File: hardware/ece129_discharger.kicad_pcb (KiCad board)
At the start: 2 copper layers, 102 parts, among them J1 Conn_01x03, J10 Conn_01x02, J11 Conn_02x05_Top_Bottom, J12 Conn_01x08, J13 Conn_02x05_Top_Bottom, J14 Conn_01x02, J16 Conn_01x08, J17 Conn_01x02, J18 Conn_01x02, J19 Conn_01x04, J2 Conn_01x02, J20 Conn_01x02, J3 Conn_01x02, J4 Conn_01x02, J5 Conn_01x02, J6 Conn_01x02, J7 Conn_01x02, J8 Conn_01x02, J9 Conn_01x02, Q2 AO3400A, U1 NUCLEO-H503RB, U13 INA126U/2K5, U15 MCP6004, U16 LTC6992CS6-2-TRMPBF, U17 6N137, U2 SN74LVC1T45DBV, U3 MCP6004, U4 MCP6004, U5 CD4052B, U6 VX7805-500, U7 ISO1050DUB, U8 MCP6004, U9 CC1R5-1205SR-E

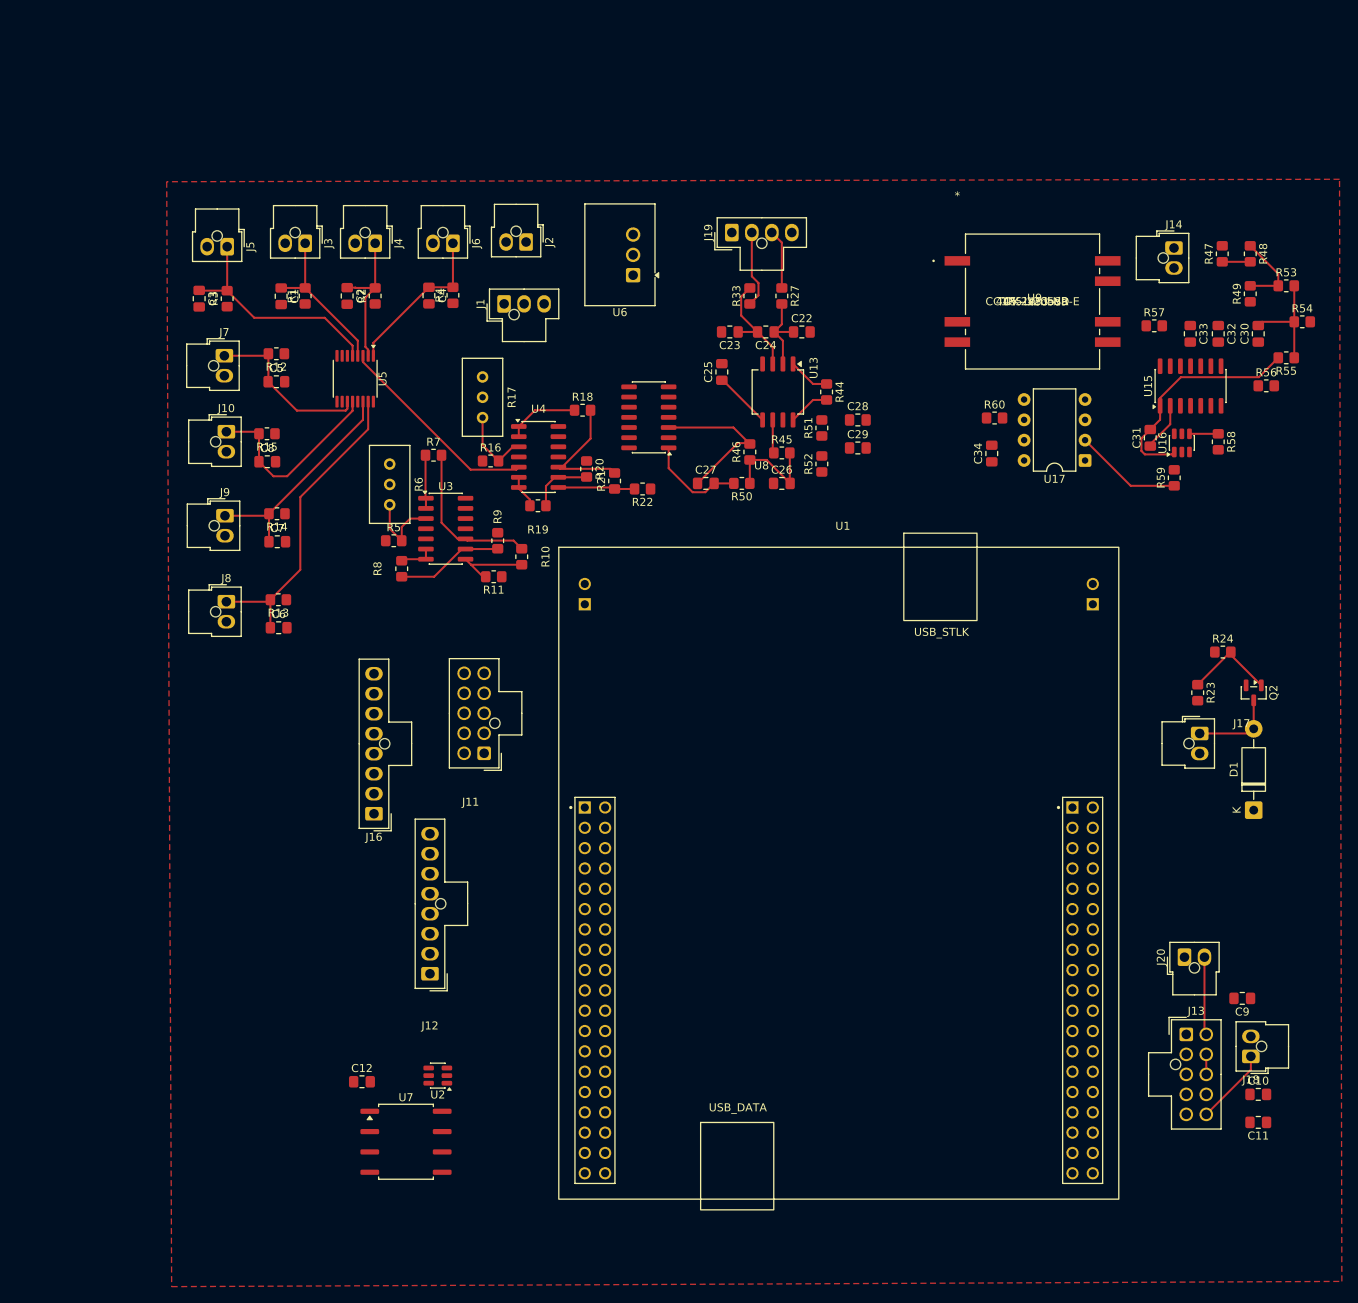
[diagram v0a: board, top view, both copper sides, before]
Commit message: Finished Layout and routing
* Flipped CAN transceiver upside down on schematic
* Moved CAN transceiver nearer to J13 and MCU CAN pins
* Moved 5V DCDC caps nearer to 5V DCDC
* Moved Silkscreen out from under U9
* Moved J2 and J1 to prevent plugging 12V into a temp sensor connector
* Change +3.3V to +3V3 to match MCU page
* Changed Current Sense circuit to use U4D, sharing with Temp Sense (for easier assembly)
* Placed Unused MCP6004s on schematic and connected them per datasheet fig 4-5
* Remove connections to HV- in Current Sensing (Replaced with GND)
* Tightened up Temp and Current Sense amplifier layouts
* Swap U15A with U15D for easier routing
* Added buffer to voltage sense circuit because filter stage could significantly load the voltage divider
* Added a smattering of decoupling caps
* Finished Layout and routing
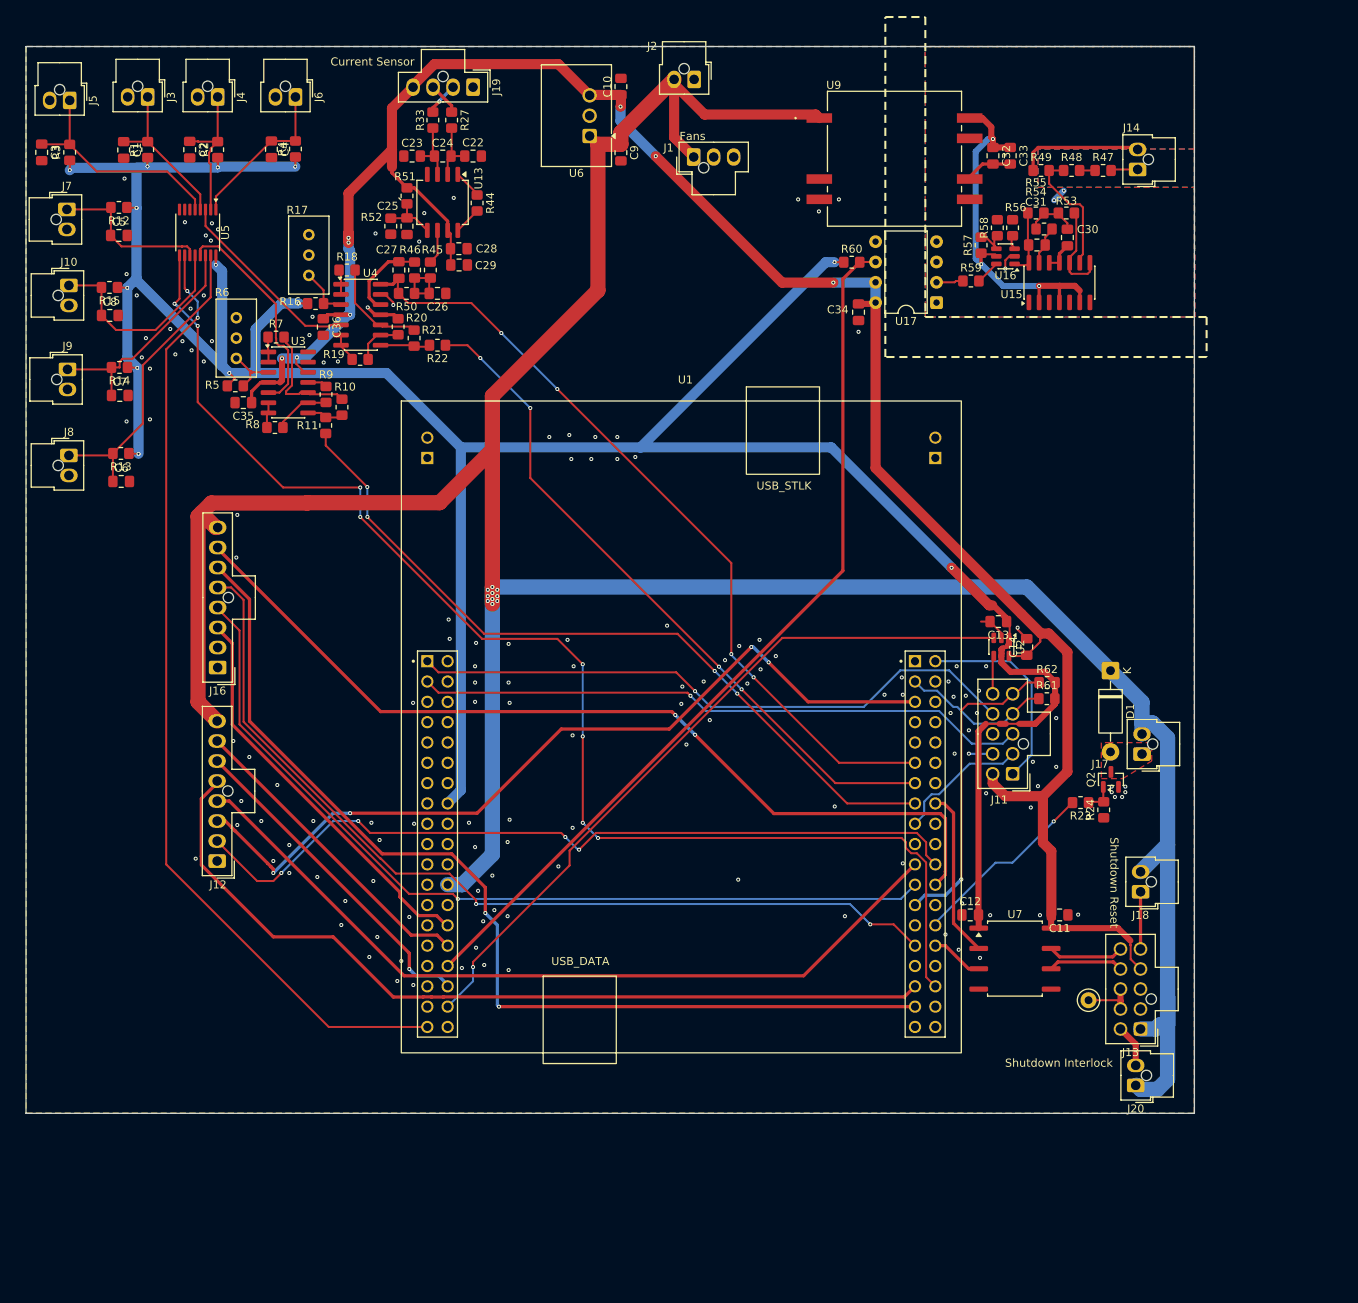
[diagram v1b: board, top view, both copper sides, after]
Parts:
- removed U8: MCP6004, Package_SO:SOIC-14_3.9x8.7mm_P1.27mm
- added C13: 100nF, Capacitor_SMD:C_0805_2012Metric_Pad1.18x1.45mm_HandSolder, F.Cu at (146.9, 97.3)
- added C14: 100nF, Capacitor_SMD:C_0805_2012Metric_Pad1.18x1.45mm_HandSolder, F.Cu at (150.5, 100.5)
- added C35: 0.1uF, Capacitor_SMD:C_0805_2012Metric_Pad1.18x1.45mm_HandSolder, F.Cu at (52.6, 69.9)
- added C36: 0.1uF, Capacitor_SMD:C_0805_2012Metric_Pad1.18x1.45mm_HandSolder, F.Cu at (62.6, 60.5)
- added R61: 6.8k, Resistor_SMD:R_0805_2012Metric_Pad1.20x1.40mm_HandSolder, F.Cu at (153.0, 106.9)
- added R62: 6.8k, Resistor_SMD:R_0805_2012Metric_Pad1.20x1.40mm_HandSolder, F.Cu at (153.0, 104.9)
- added REF**: TestPoint_Keystone_5000-5004_Miniature, TestPoint:TestPoint_Keystone_5000-5004_Miniature, F.Cu at (158.2, 144.6)
- moved C10 149.1 mm to (99.8, 30.4), turned to 90 degrees
- moved C9 131.2 mm to (99.8, 38.7), turned to -90 degrees
- moved U2 88.5 mm to (147.3, 100.5), turned to -90 degrees
- moved U7 79.5 mm to (149.0, 139.4)
- moved C12 78.8 mm to (143.4, 134.0)
- moved J11 66.1 mm to (148.7, 116.3)
- moved R52 61.5 mm to (71.0, 47.9)
- moved R51 59.4 mm to (73.0, 44.1)
- moved C29 54.8 mm to (79.5, 52.7)
- moved C28 54.3 mm to (79.5, 50.7)
- moved R44 49.7 mm to (81.8, 45.0)
- moved R45 49.5 mm to (75.9, 53.3), turned to -90 degrees
- moved C26 49.2 mm to (76.8, 56.3), turned to 180 degrees
- moved R50 48.2 mm to (73.0, 56.3)
- moved U13 48.1 mm to (77.5, 44.9)
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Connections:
- C12 pad 2: +3.3V -> +3V3
- C26 pad 1: HV_- -> GND
- C27 pad 1: Net-(U8A-+) -> Net-(U4D-+)
- C31 pad 1: Net-(U15A--) -> Net-(U15D--)
- J13 pad 10: Net-(J13-Pin_10) -> CAN_H
- J13 pad 4: /CAN_L1 -> +5V
- J13 pad 5: /CAN_H1 -> /Shutdown_Reset
- J13 pad 9: +5V -> CAN_L
- J18 pad 1: Net-(J13-Pin_10) -> /Shutdown_Reset
- R46 pad 2: Net-(U8A-+) -> Net-(U4D-+)
- R48 pad 1: Net-(R48-Pad1) -> Net-(U15C--)
- R49 pad 2: Net-(R48-Pad1) -> Net-(U15C--)
- R53 pad 1: Net-(R48-Pad1) -> Net-(U15C-+)
- R54 pad 2: Net-(U15A--) -> Net-(U15D--)
- R60 pad 1: +3.3V -> +3V3
- U1 pad CN10_13: /Microcontroller/TempSensing1 -> /Microcontroller/TempSensing2
- U1 pad CN10_15: /Microcontroller/TempSensing2 -> /Microcontroller/TempSensing1
- U1 pad CN10_29: /Microcontroller/~{RB_GATE_FAULT} -> /Microcontroller/RP_GATE_READY
- U1 pad CN10_33: /Microcontroller/RP_GATE_READY -> /Microcontroller/~{RB_GATE_FAULT}
- U1 pad CN7_1: /Microcontroller/ENC_BUTTON -> /Microcontroller/START_BUTTON
- U1 pad CN7_24: unconnected-(U1B-VIN-PadCN7_24) -> +12V
- U1 pad CN7_3: /Microcontroller/START_BUTTON -> /Microcontroller/ENC_BUTTON
- U1 pad CN7_5: +12V -> unconnected-(U1B-VDD-PadCN7_5)
- U15 pad 1: Net-(U16-MOD) -> /Voltage Sense Amplifier1/Net-(U15D-+)
- U15 pad 10: (no net) -> Net-(U15C-+)
- U15 pad 12: (no net) -> HV_-
- U15 pad 13: (no net) -> Net-(U15D--)
- U15 pad 14: (no net) -> Net-(U16-MOD)
- U15 pad 2: Net-(U15A--) -> +5V_isolated
- U15 pad 5: (no net) -> HV_-
- U15 pad 6: (no net) -> +5V_isolated
- U15 pad 7: (no net) -> unconnected-(U15-Pad7)
- U15 pad 8: (no net) -> Net-(U15C-+)
- U15 pad 9: (no net) -> Net-(U15C--)
- U3 pad 12: (no net) -> +5V
- U3 pad 13: (no net) -> GND
- U3 pad 14: (no net) -> unconnected-(U3-Pad14)
- U4 pad 12: (no net) -> Net-(U4D-+)
- U4 pad 13: (no net) -> GND
- U4 pad 14: (no net) -> /Microcontroller/BUS_CURRENT
- U7 pad 1: +3.3V -> +3V3
- U7 pad 6: /CAN_L1 -> CAN_L
- U7 pad 7: /CAN_H1 -> CAN_H
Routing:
- net +12V: track 0.00 -> 377.4 mm, vias 0 -> 10
- net +3V3: track 0.00 -> 369.0 mm, vias 0 -> 13
- net +5V: track 0.00 -> 273.8 mm, vias 0 -> 8
- net /Microcontroller/TempSensing1_B: track 0.00 -> 164.9 mm, vias 0 -> 8
- net /Microcontroller/~{RP_GATE_RESET}: track 0.00 -> 126.7 mm, vias 0 -> 2
- net /Microcontroller/TempSensing1_A: track 0.00 -> 119.5 mm, vias 0 -> 2
- net /Microcontroller/RP_GATE_READY: track 0.00 -> 115.1 mm, vias 0 -> 2
- net /Microcontroller/RP_GATE_PWM: track 0.00 -> 113.9 mm, vias 0 -> 2
- net /Microcontroller/BUS_VOLTAGE_PWM: track 0.00 -> 111.3 mm
- net /Microcontroller/~{RP_GATE_FAULT}: track 0.00 -> 110.0 mm, vias 0 -> 1
- net /Microcontroller/~{RB_GATE_FAULT}: track 0.00 -> 107.9 mm
- net /Microcontroller/~{RB_GATE_RST}: track 0.00 -> 104.8 mm, vias 0 -> 4
- net /Microcontroller/RB_GATE_PWM: track 0.00 -> 102.1 mm
- net /Microcontroller/~{RB_GATE_RESET_STATUS}: track 0.00 -> 99.9 mm, vias 0 -> 4
- net /Microcontroller/TempSensing1: track 0.00 -> 95.9 mm, vias 0 -> 4
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- added copper zone on B.Cu, net GND
- added copper zone on B.Cu, net HV_-
- added copper zone on F.Cu, net HV_-
- added copper zone on F.Cu, net Net-(D1-A)
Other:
- board outline added: 146 x 133.3 mm

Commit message: Fix up silkscreen, testpoints, and one more decoupler
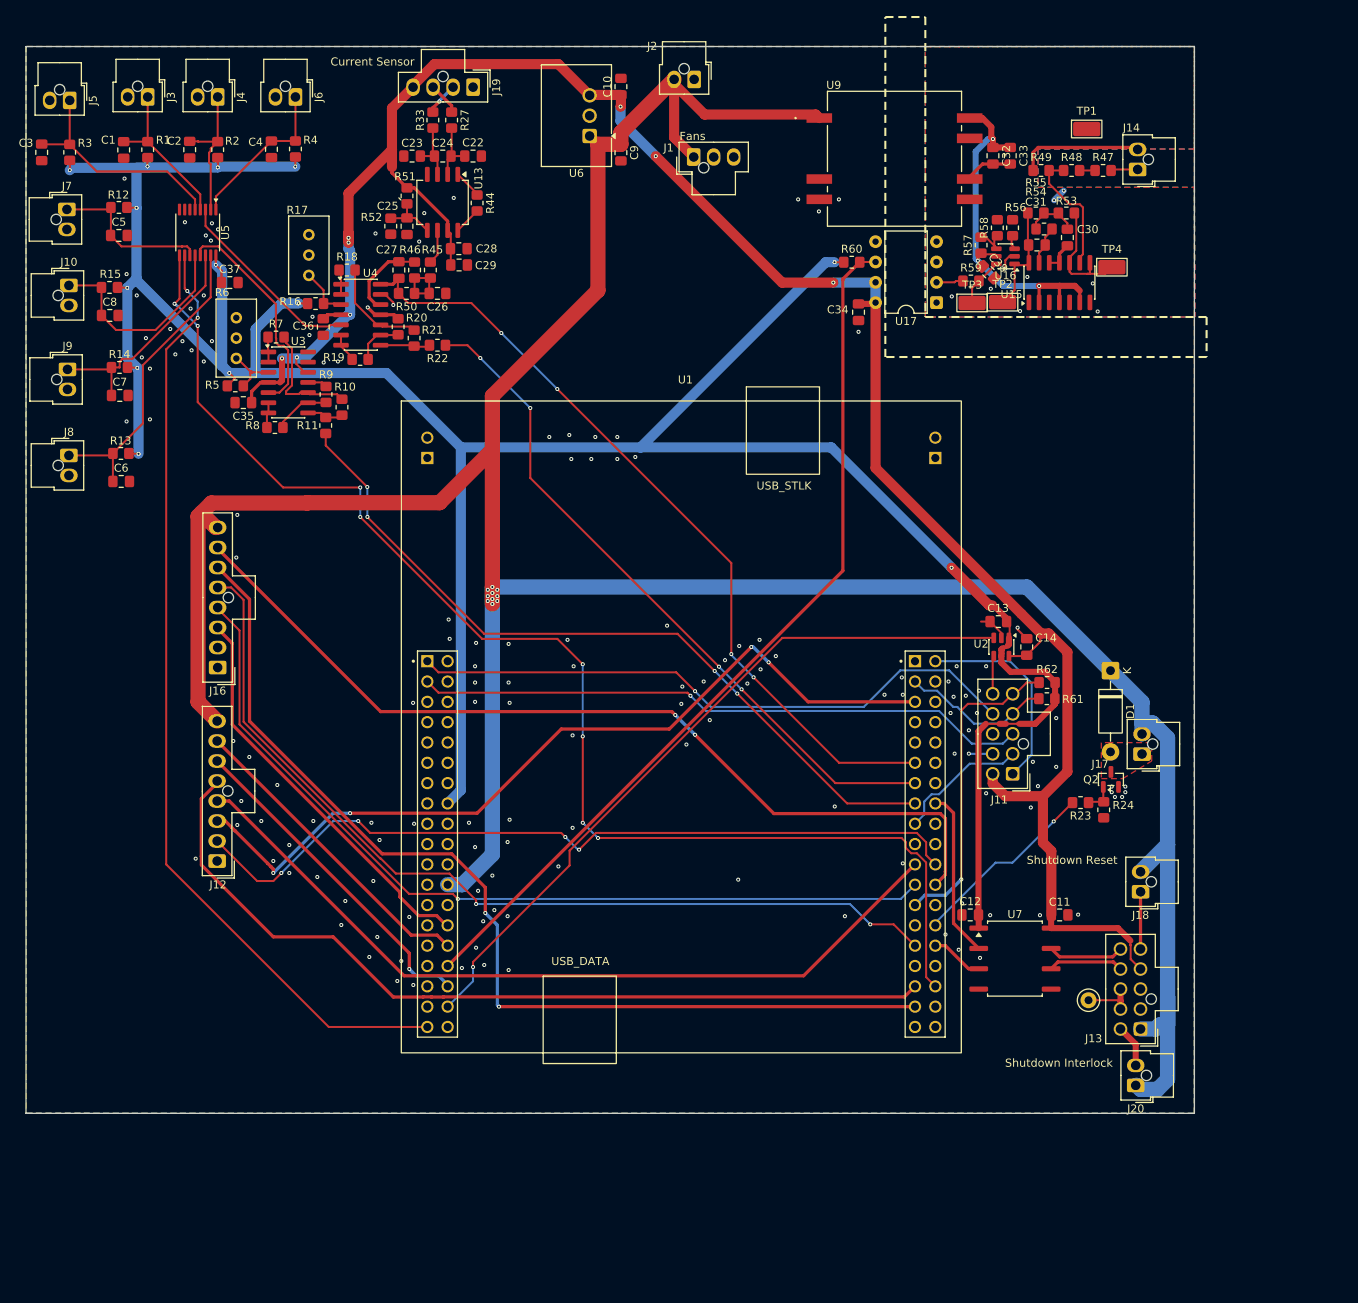
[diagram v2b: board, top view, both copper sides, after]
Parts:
- added C37: 0.1uF, Capacitor_SMD:C_0805_2012Metric_Pad1.18x1.45mm_HandSolder, F.Cu at (50.9, 54.9)
- added C38: 0.1uF, Capacitor_SMD:C_0805_2012Metric_Pad1.18x1.45mm_HandSolder, F.Cu at (145.7, 53.6)
- added TP1: HV-, TestPoint:TestPoint_Keystone_5015_Micro_Mini, F.Cu at (158.0, 35.7)
- added TP2: HV_Mod, TestPoint:TestPoint_Keystone_5015_Micro_Mini, F.Cu at (147.5, 57.4)
- added TP3: HV_PWM, TestPoint:TestPoint_Keystone_5015_Micro_Mini, F.Cu at (143.7, 57.5)
- added TP4: HV_Sense_buf, TestPoint:TestPoint_Keystone_5015_Micro_Mini, F.Cu at (161.1, 53.0)
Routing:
- net Net-(U16-MOD): track 7.86 -> 13.3 mm
- net Net-(U15C-+): track 10.5 -> 14.0 mm
- net Net-(U16-OUT): track 3.02 -> 6.11 mm
- net +3V3: track 369.0 -> 371.5 mm
- net HV_-: vias 3 -> 9

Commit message: final rev 1.0 complete
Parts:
- moved C38 5.24 mm to (141.5, 50.5), turned to 90 degrees
- moved C12 2.56 mm to (145.5, 132.5), turned to 180 degrees
- moved R59 1.01 mm to (142.5, 54.7)
- moved TP4 0.86 mm to (162.0, 53.0)
- moved TP3 0.66 mm to (143.0, 57.5)
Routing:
- net +5V_isolated: track 48.7 -> 51.5 mm
- net Net-(U16-OUT): track 6.11 -> 7.97 mm
- net Net-(U17-A): track 3.37 -> 2.35 mm
- net Net-(U15C-+): track 14.0 -> 14.9 mm
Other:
- board size 146 x 133.3 mm -> 146 x 134.2 mm
- board text added: "Discharger Main Board Rev. 1.0 Schematic & Layout: Maitreyi Patel & Wesley Rodriguez Kronmiller"
